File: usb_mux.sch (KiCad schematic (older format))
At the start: 2 parts, among them U19 FSUSB42MUX, U20 FSUSB42MUX

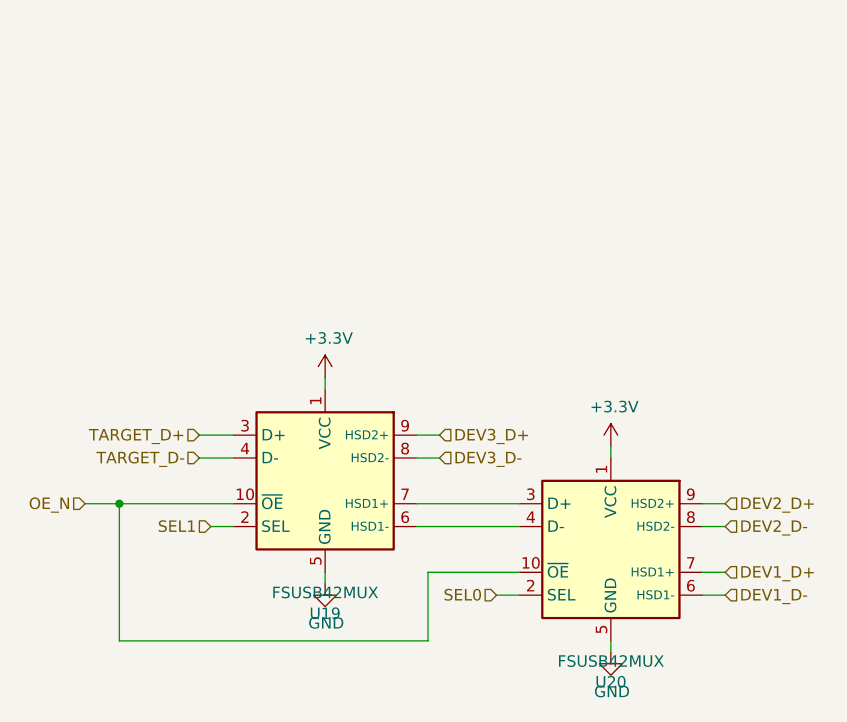
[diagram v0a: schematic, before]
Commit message: Supply caps, initial signal states and headers
  * Added bulk supply caps.
  * Set initial control signal states via resistors.
  * Add debug headers.
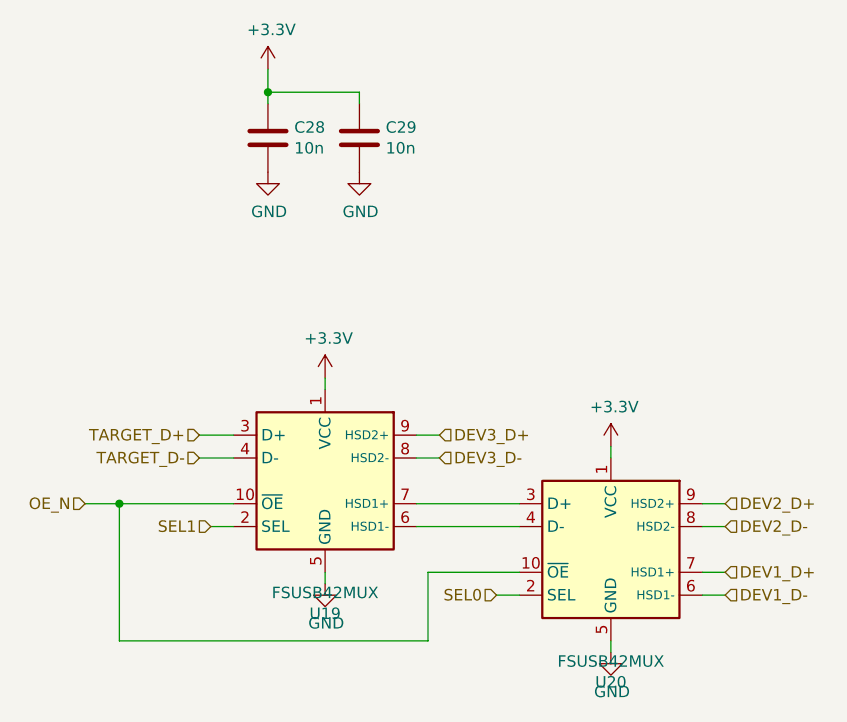
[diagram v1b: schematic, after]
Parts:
- added C28, C29: 10n, symbol Device:C
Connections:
- net +3V3: now also C28.1, C29.1
- net GND: now also C28.2, C29.2
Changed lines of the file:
@@
 	1    0    0    -1
 $EndComp
+$Comp
+L Device:C C28
+U 1 1 61B6FDF2
+P 5550 2400
+F 0 "C28" H 5665 2446 50  0000 L CNN
+F 1 "10n" H 5665 2355 50  0000 L CNN
+F 2 "" H 5588 2250 50  0001 C CNN
+F 3 "~" H 5550 2400 50  0001 C CNN
+	1    5550 2400
+	1    0    0    -1
+$EndComp
+$Comp
+L power:GND #PWR0152
+U 1 1 61B6FDF8
+P 5550 2550
+F 0 "#PWR0152" H 5550 2300 50  0001 C CNN
+F 1 "GND" H 5555 2377 50  0000 C CNN
+F 2 "" H 5550 2550 50  0001 C CNN
+F 3 "" H 5550 2550 50  0001 C CNN
+	1    5550 2550
+	1    0    0    -1
+$EndComp
+$Comp
+L power:+3.3V #PWR0153
+U 1 1 61B6FDFE
+P 5550 2100
+F 0 "#PWR0153" H 5550 1950 50  0001 C CNN
+F 1 "+3.3V" H 5565 2273 50  0000 C CNN
+F 2 "" H 5550 2100 50  0001 C CNN
+F 3 "" H 5550 2100 50  0001 C CNN
+	1    5550 2100
+	1    0    0    -1
+$EndComp
+$Comp
+L Device:C C29
+U 1 1 61B6FE04
+P 5950 2400
+F 0 "C29" H 6065 2446 50  0000 L CNN
+F 1 "10n" H 6065 2355 50  0000 L CNN
+F 2 "" H 5988 2250 50  0001 C CNN
+F 3 "~" H 5950 2400 50  0001 C CNN
+	1    5950 2400
+	1    0    0    -1
+$EndComp
+$Comp
+L power:GND #PWR0154
+U 1 1 61B6FE0A
+P 5950 2550
+F 0 "#PWR0154" H 5950 2300 50  0001 C CNN
+F 1 "GND" H 5955 2377 50  0000 C CNN
+F 2 "" H 5950 2550 50  0001 C CNN
+F 3 "" H 5950 2550 50  0001 C CNN
+	1    5950 2550
+	1    0    0    -1
+$EndComp
+Wire Wire Line
+	5550 2200 5550 2100
+Wire Wire Line
+	5550 2200 5550 2250
+Connection ~ 5550 2200
+Wire Wire Line
+	5950 2200 5950 2250
+Wire Wire Line
+	5950 2200 5550 2200
 $EndSCHEMATC
